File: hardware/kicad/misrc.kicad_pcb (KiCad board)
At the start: 2 copper layers, 146.2 x 72.6 mm, 177 parts, among them J1 Conn_01x01_Shielded, J101 BNC_Rosenberger, J2 Conn_01x08_Socket, J201 BNC_Rosenberger, J3 GPIFII_J6, J4 GPIFII_J7, Q1 FZT690B, Q2 FZT790A, SW1 SW_Push, SW101 SW_DIP_x04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

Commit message: new hardware revision
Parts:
- added C127: 10µ, Capacitor_SMD:C_0805_2012Metric, F.Cu at (80.5, 118.0)
- added C128: 1n, Capacitor_SMD:C_0805_2012Metric, F.Cu at (82.7, 118.0)
- added C227: 10µ, Capacitor_SMD:C_0805_2012Metric, F.Cu at (80.4, 83.5)
- added C228: 1n, Capacitor_SMD:C_0805_2012Metric, F.Cu at (82.5, 83.5)
- added C27: 1n, Capacitor_SMD:C_0805_2012Metric, B.Cu at (181.5, 70.8)
- added C28: 10µ, Capacitor_SMD:C_0805_2012Metric, B.Cu at (183.6, 70.8)
- added C29: 1µ, Capacitor_SMD:C_0805_2012Metric, B.Cu at (73.0, 91.3)
- added C30: 1µ, Capacitor_SMD:C_0805_2012Metric, B.Cu at (82.7, 124.8)
- added C31: 1µ, Capacitor_SMD:C_0805_2012Metric, B.Cu at (147.4, 93.3)
- added Q101: CMPT5179, Package_TO_SOT_SMD:SOT-23-3, B.Cu at (92.8, 113.3)
- added Q102: CMPT5179, Package_TO_SOT_SMD:SOT-23-3, B.Cu at (92.3, 109.4)
- added Q201: CMPT5179, Package_TO_SOT_SMD:SOT-23-3, B.Cu at (92.8, 78.9)
- added Q202: CMPT5179, Package_TO_SOT_SMD:SOT-23-3, B.Cu at (92.3, 75.1)
- added R127: 3k3, Resistor_SMD:R_0805_2012Metric, F.Cu at (78.2, 119.9)
- added R228: 3k3, Resistor_SMD:R_0805_2012Metric, F.Cu at (78.2, 85.5)
- added SW2: SW_DIP_x01, Button_Switch_SMD:SW_DIP_SPSTx01_Slide_6.7x4.1mm_W8.61mm_P2.54mm_LowProfile, F.Cu at (150.0, 101.7)
- added X1: 40M, Oscillator:Oscillator_SMD_EuroQuartz_XO53-4Pin_5.0x3.2mm, B.Cu at (150.7, 94.2)
- C101, C201: value 22µ -> 100µ
- C105, C205: value 100n -> 470n
- R101, R102, R201, R202: value 150 -> 75
- R106, R108, R206, R208: value 75 -> 39
- R111, R118, R211, R218: value 1k3 -> 1k
- moved R104 26.7 mm to (111.8, 113.5)
- moved R204 26.6 mm to (112.1, 85.1)
- moved R105 19.0 mm to (109.6, 113.5), turned to -90 degrees
- moved R205 17.2 mm to (110.0, 85.1)
- moved C202 16.7 mm to (110.9, 80.4), turned to 90 degrees
- moved C102 14.9 mm to (110.4, 118.0)
- moved C203 11.5 mm to (108.2, 81.2), turned to 90 degrees
- moved C103 10.9 mm to (107.4, 115.7), turned to 90 degrees
- moved C204 8.59 mm to (106.2, 81.2), turned to 90 degrees
- moved C104 8.15 mm to (105.4, 115.7), turned to 90 degrees
- moved C222 3.41 mm to (101.1, 83.4), turned to 0 degrees
- moved RV201 1.34 mm to (75.7, 91.3)
- moved RV101 1.30 mm to (75.7, 125.7)
- moved C122 1.05 mm to (101.0, 117.9)
- moved C3 0.80 mm to (151.8, 109.5)
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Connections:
- J3 pad 33: unconnected-(J3-GND-Pad33) -> GND
- R108 pad 2: GND -> Net-(C127-Pad1)
- R208 pad 2: GND -> Net-(C227-Pad1)
- RV101 pad 1: GND -> -5VA
- RV101 pad 2: GND -> Net-(R127-Pad2)
- RV101 pad 3: Net-(RV101-Pad3) -> +5VA
- RV201 pad 1: GND -> -5VA
- RV201 pad 2: GND -> Net-(R228-Pad2)
- RV201 pad 3: Net-(RV201-Pad3) -> +5VA
- SW102 pad 1: GND -> Net-(C127-Pad1)
- SW102 pad 2: GND -> Net-(C127-Pad1)
- SW102 pad 3: Net-(RV101-Pad3) -> Net-(C127-Pad1)
- SW102 pad 4: Net-(U101-VCM) -> GND
- SW202 pad 1: GND -> Net-(C227-Pad1)
- SW202 pad 2: GND -> Net-(C227-Pad1)
- SW202 pad 3: Net-(RV201-Pad3) -> Net-(C227-Pad1)
- SW202 pad 4: Net-(U201-VCM) -> GND
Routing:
- net -5VA: track 153.0 -> 223.0 mm
- net +5VA: track 153.3 -> 223.2 mm
- net VDDA: track 139.7 -> 88.7 mm
- net Net-(C227-Pad1): track 0.00 -> 17.4 mm
- net Net-(C127-Pad1): track 0.00 -> 16.9 mm
- net VDD: track 218.4 -> 229.7 mm
- net Net-(U201-VCM): track 24.8 -> 16.4 mm, vias 2 -> 1
- net Net-(U101-VCM): track 24.8 -> 16.4 mm, vias 2 -> 1
- net Net-(RV101-Pad3): track 8.03 -> 0.00 mm
- net Net-(RV201-Pad3): track 8.03 -> 0.00 mm
- net Net-(Q101-C): track 0.00 -> 5.51 mm
- net Net-(Q201-C): track 0.00 -> 5.40 mm
- net GND: track 32.8 -> 29.3 mm, vias 308 -> 311
- net /Input_ADC_CH1/CLK: track 135.1 -> 138.2 mm
- net Net-(R228-Pad2): track 0.00 -> 2.39 mm
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
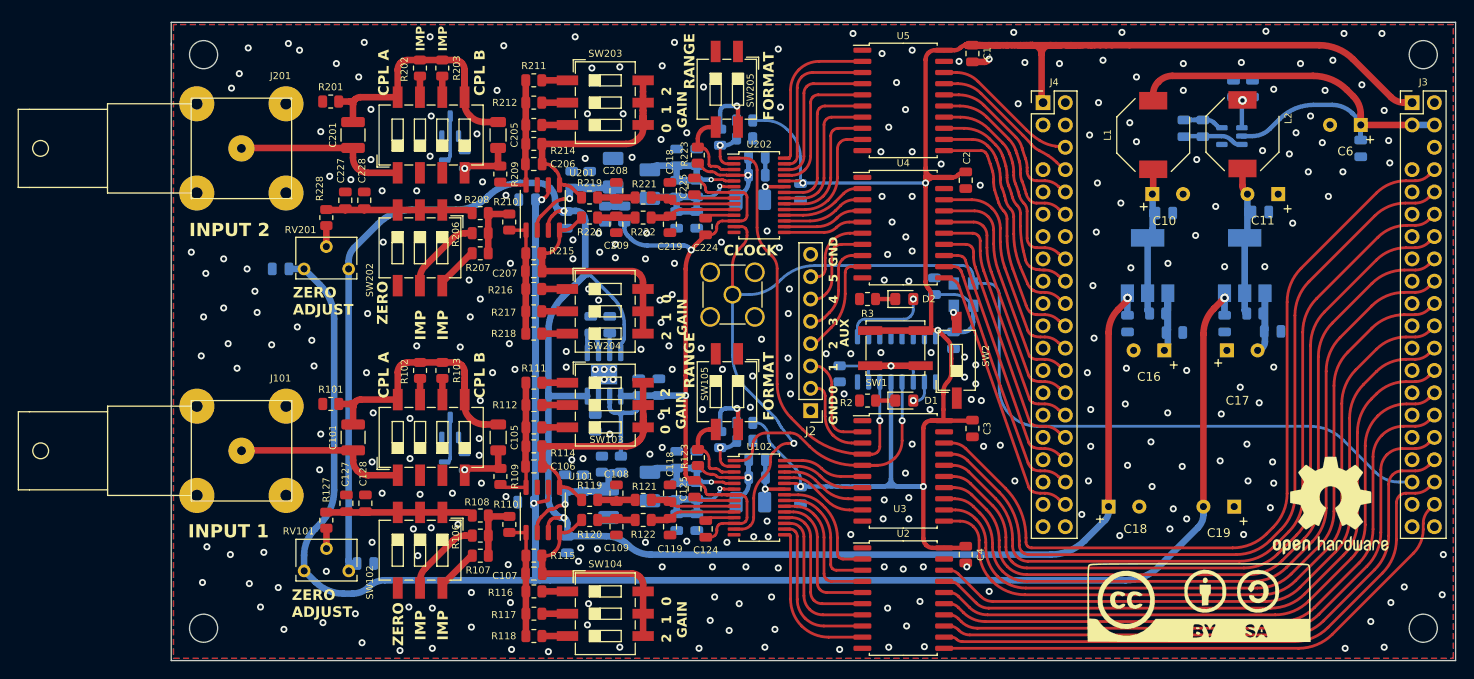
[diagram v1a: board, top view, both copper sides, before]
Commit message: Updated annonation on the PCB, added gerbers, PDFs and BOM
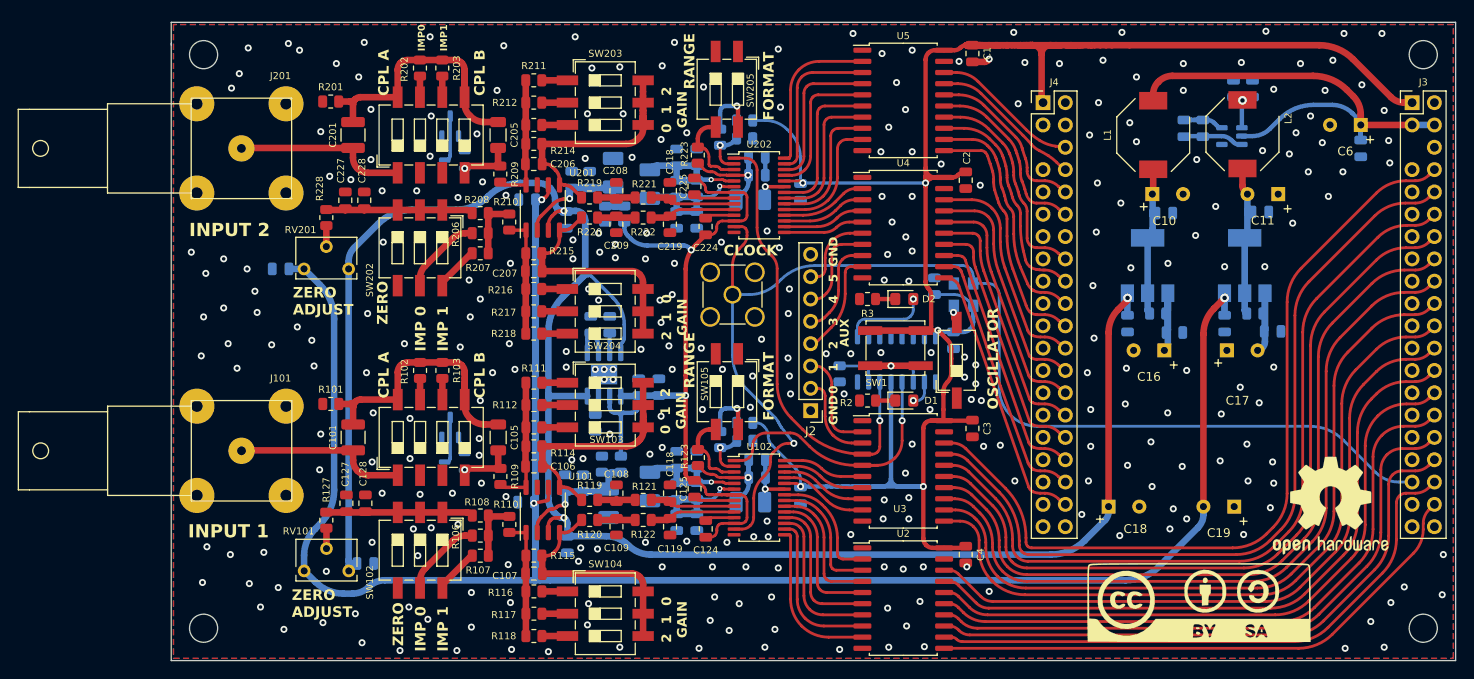
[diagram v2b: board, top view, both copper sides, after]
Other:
- board text added: "IMP 0"
- board text added: "IMP 1"
- board text added: "IMP0"
- board text added: "IMP1"
- board text added: "OSCILLATOR"
- board text removed: "IMP"
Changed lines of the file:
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@@
     (pad_to_mask_clearance 0)
     (pcbplotparams
-      (layerselection 0x00010f0_ffffffff)
-      (plot_on_all_layers_selection 0x0000000_00000000)
+      (layerselection 0x00010ff_ffffffff)
+      (plot_on_all_layers_selection 0x0001000_00000000)
       (disableapertmacros false)
       (usegerberextensions false)
@@
       (dashed_line_gap_ratio 3.000000)
       (svgprecision 4)
-      (plotframeref false)
+      (plotframeref true)
       (viasonmask false)
       (mode 1)
@@
       (drillshape 0)
       (scaleselection 1)
-      (outputdirectory "gerber/")
+      (outputdirectory "../PDF/")
     )
   )
@@
     (property "ki_keywords" "dip switch")
     (attr smd)
-    (fp_text reference "SW2" (at 0.508 3.302 90) (layer "F.SilkS")
+    (fp_text reference "SW2" (at 0.508 3.302 90) (layer "F.SilkS") hide
         (effects (font (size 0.8 0.8) (thickness 0.12)))
     )
@@
     (fp_line (start 1 0.625) (end -1 0.625)
       (stroke (width 0.1) (type solid)) (layer "F.Fab"))
-    (pad "1" smd roundrect (at -0.9125 0 270) (size 1.025 1.4) (layers "F.Cu" "F.Paste" "F.Mask") (roundrect_rratio 0.243902)
+    (pad "1" smd roundrect (at -0.9125 0 270) (size 1.025 1.4) (layers "F.Cu" "F.Paste" "F.Mask") (roundrect_rratio 0.243902439)
       (net 81 "Net-(C227-Pad1)") (pintype "passive"))
-    (pad "2" smd roundrect (at 0.9125 0 270) (size 1.025 1.4) (layers "F.Cu" "F.Paste" "F.Mask") (roundrect_rratio 0.243902)
+    (pad "2" smd roundrect (at 0.9125 0 270) (size 1.025 1.4) (layers "F.Cu" "F.Paste" "F.Mask") (roundrect_rratio 0.243902439)
       (net 183 "Net-(R228-Pad2)") (pintype "passive"))
     (model "${KICAD6_3DMODEL_DIR}/Resistor_SMD.3dshapes/R_0805_2012Metric.wrl"
@@
     (fp_line (start 1 0.625) (end -1 0.625)
       (stroke (width 0.1) (type solid)) (layer "F.Fab"))
-    (pad "1" smd roundrect (at -0.9125 0 270) (size 1.025 1.4) (layers "F.Cu" "F.Paste" "F.Mask") (roundrect_rratio 0.243902)
+    (pad "1" smd roundrect (at -0.9125 0 270) (size 1.025 1.4) (layers "F.Cu" "F.Paste" "F.Mask") (roundrect_rratio 0.243902439)
       (net 65 "Net-(C127-Pad1)") (pintype "passive"))
-    (pad "2" smd roundrect (at 0.9125 0 270) (size 1.025 1.4) (layers "F.Cu" "F.Paste" "F.Mask") (roundrect_rratio 0.243902)
+    (pad "2" smd roundrect (at 0.9125 0 270) (size 1.025 1.4) (layers "F.Cu" "F.Paste" "F.Mask") (roundrect_rratio 0.243902439)
       (net 172 "Net-(R127-Pad2)") (pintype "passive"))
     (model "${KICAD6_3DMODEL_DIR}/Resistor_SMD.3dshapes/R_0805_2012Metric.wrl"
@@
   (gr_line (start 60.579 63.246) (end 60.579 65.659)
     (stroke (width 0.1) (type default)) (layer "Edge.Cuts"))
-  (gr_text "IMP\n" (at 92.202 133.604 90) (layer "F.SilkS")
+  (gr_text "IMP 1" (at 92.202 134.874 90) (layer "F.SilkS")
     (effects (font (size 1.2 1.2) (thickness 0.25) bold) (justify left bottom))
   )
@@
     (effects (font (size 1.5 1.5) (thickness 0.3) bold) (justify left bottom))
   )
-  (gr_text "IMP\n" (at 92.202 99.441 90) (layer "F.SilkS")
+  (gr_text "IMP 1" (at 92.202 100.711 90) (layer "F.SilkS")
     (effects (font (size 1.2 1.2) (thickness 0.25) bold) (justify left bottom))
   )
@@
     (effects (font (size 1 1) (thickness 0.2) bold) (justify left bottom))
   )
-  (gr_text "IMP" (at 89.535 66.548 90) (layer "F.SilkS")
-    (effects (font (size 1 1) (thickness 0.2) bold) (justify left bottom))
+  (gr_text "IMP0" (at 89.535 66.548 90) (layer "F.SilkS")
+    (effects (font (size 0.8 0.8) (thickness 0.16) bold) (justify left bottom))
   )
   (gr_text "0  1  2\n GAIN" (at 119.253 110.109 90) (layer "F.SilkS")
@@
     (effects (font (size 1.2 1.2) (thickness 0.25) bold) (justify left bottom))
   )
-  (gr_text "IMP\n" (at 89.662 133.604 90) (layer "F.SilkS")
+  (gr_text "IMP 0" (at 89.662 134.874 90) (layer "F.SilkS")
     (effects (font (size 1.2 1.2) (thickness 0.25) bold) (justify left bottom))
   )
@@
     (effects (font (size 1.2 1.2) (thickness 0.25) bold) (justify left bottom))
   )
-  (gr_text "IMP\n" (at 89.662 99.441 90) (layer "F.SilkS")
+  (gr_text "OSCILLATOR" (at 154.813 107.315 90) (layer "F.SilkS")
+    (effects (font (size 1.2 1.2) (thickness 0.25) bold) (justify left bottom))
+  )
+  (gr_text "IMP 0" (at 89.662 100.711 90) (layer "F.SilkS")
     (effects (font (size 1.2 1.2) (thickness 0.25) bold) (justify left bottom))
   )
@@
     (effects (font (size 1.1 1.1) (thickness 0.25) bold) (justify left bottom))
   )
-  (gr_text "IMP" (at 92.075 66.548 90) (layer "F.SilkS")
-    (effects (font (size 1 1) (thickness 0.2) bold) (justify left bottom))
+  (gr_text "IMP1" (at 92.075 66.548 90) (layer "F.SilkS")
+    (effects (font (size 0.8 0.8) (thickness 0.16) bold) (justify left bottom))
   )
   (gr_text "ZERO" (at 85.344 97.663 90) (layer "F.SilkS")
@@
   (via (at 90.043 78.486) (size 0.8) (drill 0.4) (layers "F.Cu" "B.Cu") (net 2))
   (via (at 79.375 67.945) (size 0.8) (drill 0.4) (layers "F.Cu" "B.Cu") (net 2))
-  (via (at 90.297 134.493) (size 0.8) (drill 0.4) (layers "F.Cu" "B.Cu") (net 2))
+  (via (at 89.789 131.191) (size 0.8) (drill 0.4) (layers "F.Cu" "B.Cu") (net 2))
   (via (at 64.643 122.936) (size 0.8) (drill 0.4) (layers "F.Cu" "B.Cu") (net 2))
   (via (at 166.116 72.39) (size 0.8) (drill 0.4) (layers "F.Cu" "B.Cu") (net 2))
@@
   (via (at 64.262 96.774) (size 0.8) (drill 0.4) (layers "F.Cu" "B.Cu") (net 2))
   (via (at 90.17 73.914) (size 0.8) (drill 0.4) (layers "F.Cu" "B.Cu") (net 2))
-  (via (at 90.297 129.921) (size 0.8) (drill 0.4) (layers "F.Cu" "B.Cu") (net 2))
+  (via (at 93.091 134.747) (size 0.8) (drill 0.4) (layers "F.Cu" "B.Cu") (net 2))
   (via (at 199.263 79.248) (size 0.8) (drill 0.4) (layers "F.Cu" "B.Cu") (net 2))
   (via (at 128.524 121.793) (size 0.8) (drill 0.4) (layers "F.Cu" "B.Cu") (net 2))
@@
   (via (at 88.646 123.952) (size 0.8) (drill 0.4) (layers "F.Cu" "B.Cu") (net 2))
   (via (at 130.81 96.393) (size 0.8) (drill 0.4) (layers "F.Cu" "B.Cu") (net 2))
-  (via (at 88.519 100.076) (size 0.8) (drill 0.4) (layers "F.Cu" "B.Cu") (net 2))
+  (via (at 87.122 99.822) (size 0.8) (drill 0.4) (layers "F.Cu" "B.Cu") (net 2))
   (via (at 103.505 134.874) (size 0.8) (drill 0.4) (layers "F.Cu" "B.Cu") (net 2))
   (via (at 87.757 108.331) (size 0.8) (drill 0.4) (layers "F.Cu" "B.Cu") (net 2))
